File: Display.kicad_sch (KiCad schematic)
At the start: 28 parts, among them J10 Conn_01x06_MountingPin, J2 TFT_LCD, U3 MT9284, U5 TPS61169

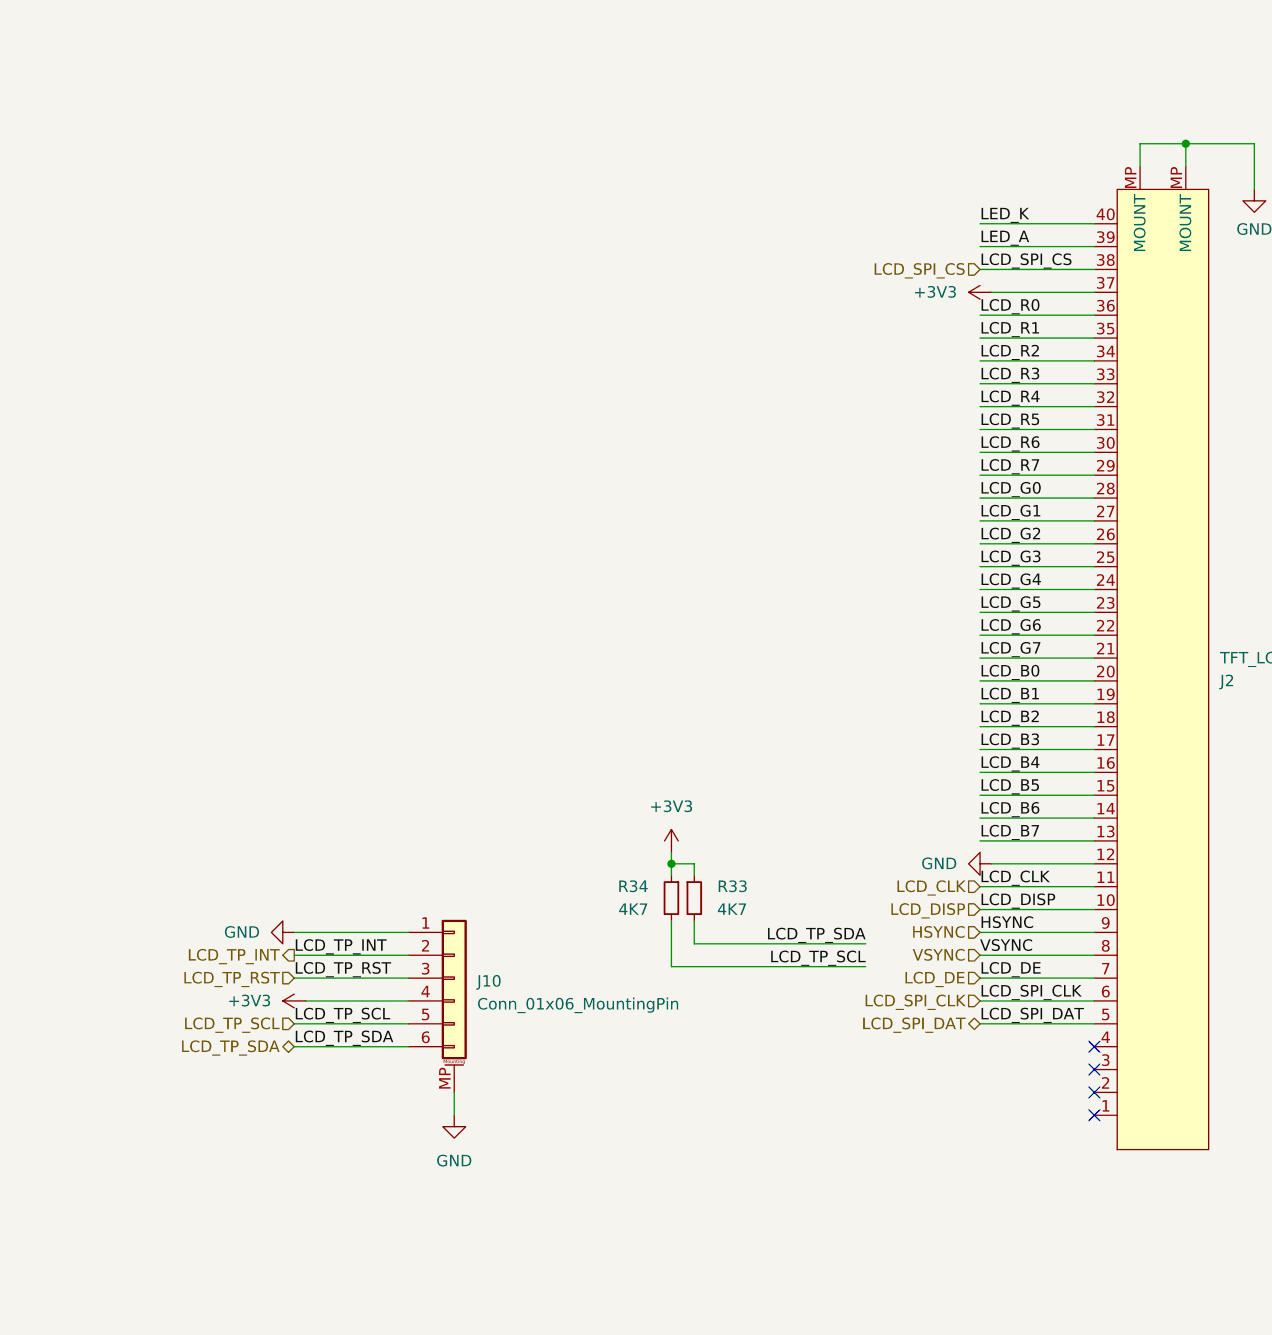
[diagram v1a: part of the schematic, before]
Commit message: Cleaning schematic, added more independently schematics
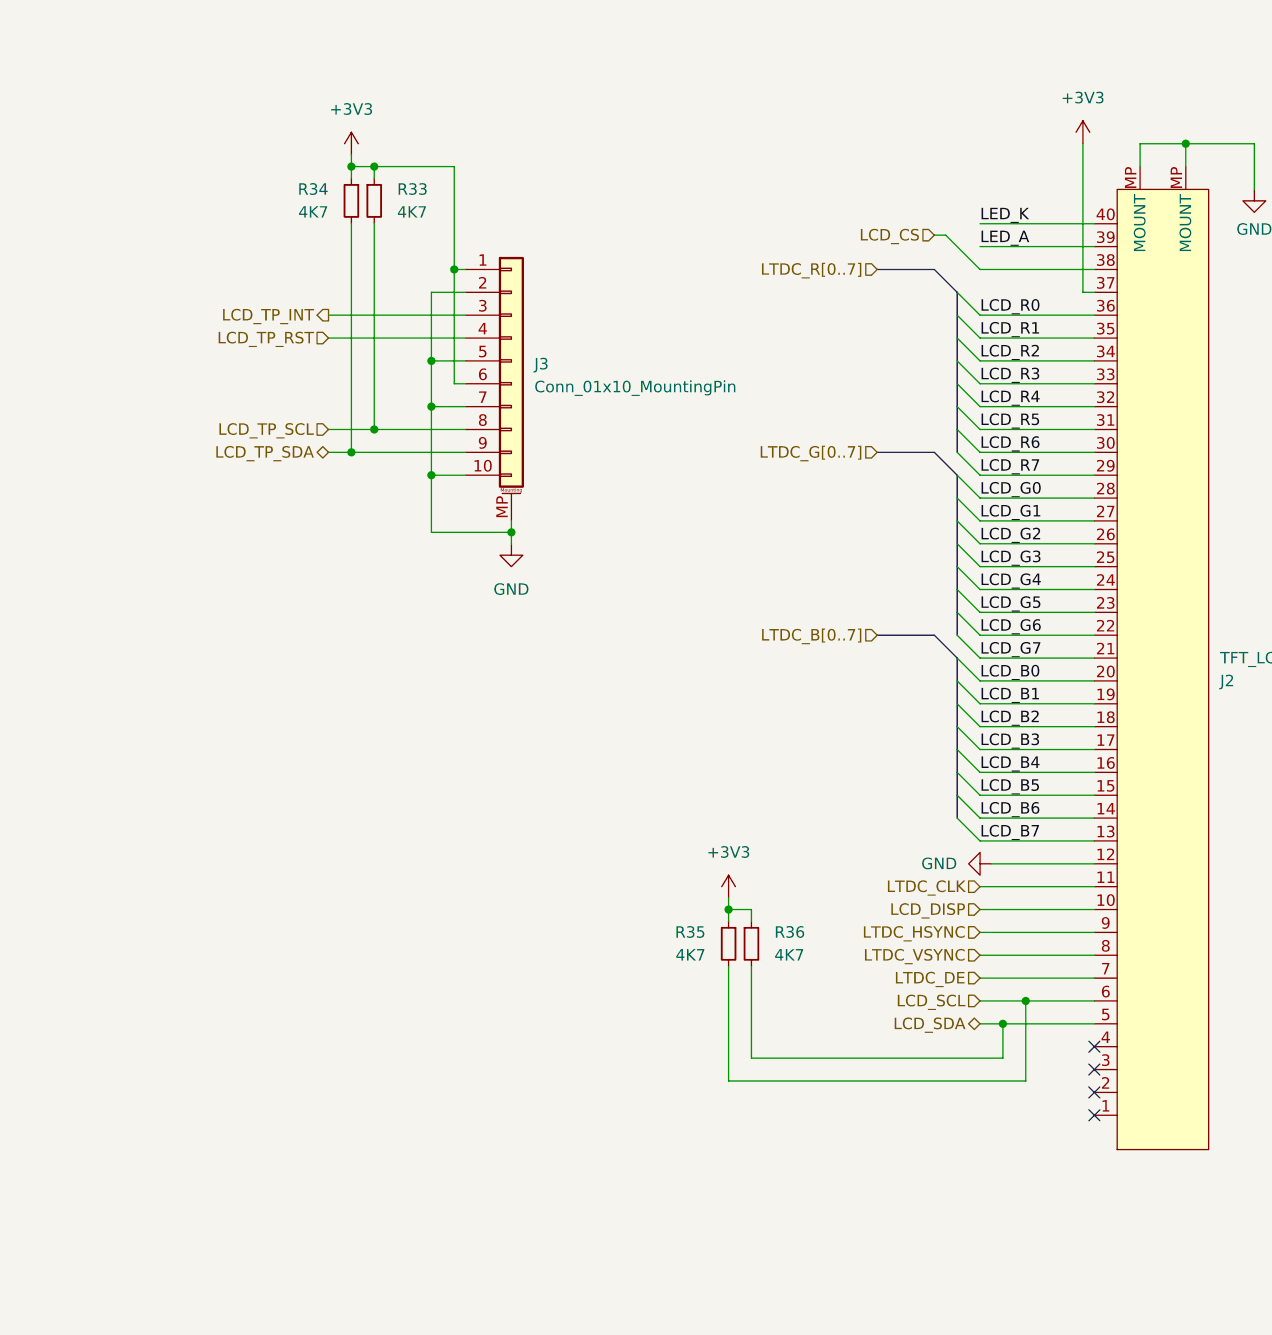
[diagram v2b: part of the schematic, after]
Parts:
- removed J10: Conn_01x06_MountingPin, Connector_FFC-FPC:TE_84953-6_1x06-1MP_P1.0mm_Horizontal, symbol Connector_Generic_MountingPin:Conn_01x06_MountingPin
- added J3: Conn_01x10_MountingPin, symbol Connector_Generic_MountingPin:Conn_01x10_MountingPin
- added R35, R36: 4K7, Resistor_SMD:R_0402_1005Metric, symbol Device:R_Small
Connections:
- net +3V3: now also J3.1 (Pin_1), J3.6 (Pin_6), R35.1, R36.1
- net GND: now also J3.10 (Pin_10), J3.2 (Pin_2), J3.5 (Pin_5), J3.7 (Pin_7), J3.MP (MountPin)
- net LCD_TP_INT: now also J3.3 (Pin_3)
- net LCD_TP_RST: now also J3.4 (Pin_4)
- net LCD_TP_SCL: now also R33.2, J3.8 (Pin_8); no longer R34.2
- net LCD_TP_SDA: now also R34.2, J3.9 (Pin_9); no longer R33.2
- net HSYNC renamed LTDC_HSYNC
- net LCD_CLK renamed LTDC_CLK
- net LCD_DE renamed LTDC_DE
- net LCD_SPI_CLK renamed LCD_SCL
- net LCD_SCL: now also R35.2
- net LCD_SPI_CS renamed LCD_CS
- net LCD_SPI_DAT renamed LCD_SDA
- net LCD_SDA: now also R36.2
- net VSYNC renamed LTDC_VSYNC
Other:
- moved on the sheet: R33, R34

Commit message: Layout SDRAM
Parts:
- J3: footprint (none) -> Connector_FFC-FPC:Hirose_FH12-10S-0.5SH_1x10-1MP_P0.50mm_Horizontal
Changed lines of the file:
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@@
 			)
 		)
-		(property "Footprint" ""
+		(property "Footprint" "Connector_FFC-FPC:Hirose_FH12-10S-0.5SH_1x10-1MP_P0.50mm_Horizontal"
 			(at 194.31 63.5 0)
 			(effects

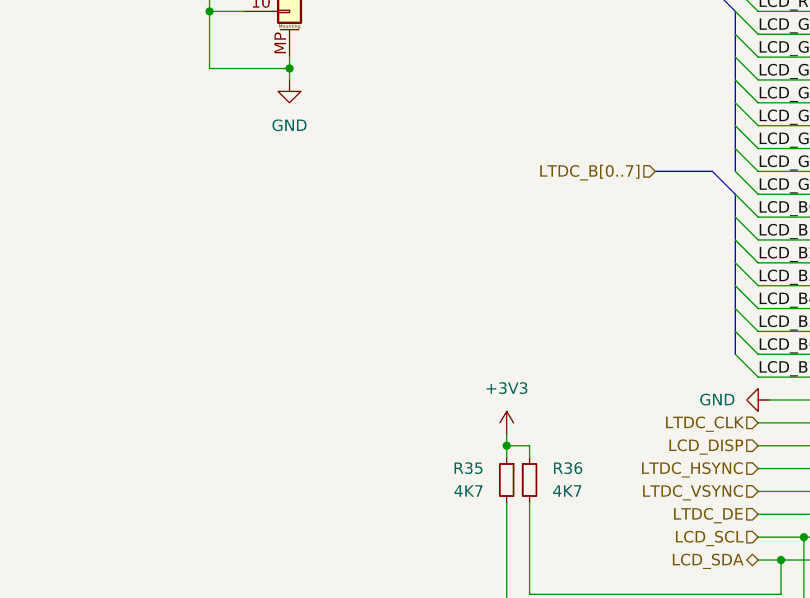
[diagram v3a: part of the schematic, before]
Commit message: relayout SDRAM
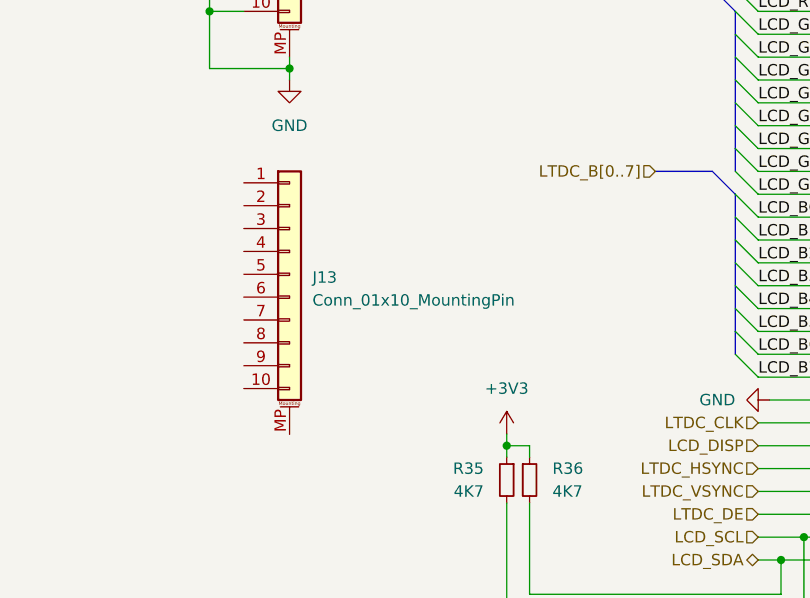
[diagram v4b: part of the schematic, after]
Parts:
- added J13: Conn_01x10_MountingPin, Connector_FFC-FPC:Hirose_FH12-10S-0.5SH_1x10-1MP_P0.50mm_Horizontal, symbol Connector_Generic_MountingPin:Conn_01x10_MountingPin
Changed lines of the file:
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@@
+	)
+	(symbol
+		(lib_id "Connector_Generic_MountingPin:Conn_01x10_MountingPin")
+		(at 194.31 105.41 0)
+		(unit 1)
+		(exclude_from_sim no)
+		(in_bom yes)
+		(on_board yes)
+		(dnp no)
+		(fields_autoplaced yes)
+		(property "Reference" "J13"
+			(at 196.85 105.7655 0)
+			(effects
+				(font
+					(size 1.27 1.27)
+				)
+				(justify left)
+			)
+		)
+		(property "Value" "Conn_01x10_MountingPin"
+			(at 196.85 108.3055 0)
+			(effects
+				(font
+					(size 1.27 1.27)
+				)
+				(justify left)
+			)
+		)
+		(property "Footprint" "Connector_FFC-FPC:Hirose_FH12-10S-0.5SH_1x10-1MP_P0.50mm_Horizontal"
+			(at 194.31 105.41 0)
+			(effects
+				(font
+					(size 1.27 1.27)
+				)
+				(hide yes)
+			)
+		)
+		(property "Datasheet" "~"
+			(at 194.31 105.41 0)
+			(effects
+				(font
+					(size 1.27 1.27)
+				)
+				(hide yes)
+			)
+		)
+		(property "Description" "Generic connectable mounting pin connector, single row, 01x10, script generated (kicad-library-utils/schlib/autogen/connector/)"
+			(at 194.31 105.41 0)
+			(effects
+				(font
+					(size 1.27 1.27)
+				)
+				(hide yes)
+			)
+		)
+		(pin "2"
+		)
+		(pin "1"
+		)
+		(pin "8"
+		)
+		(pin "3"
+		)
+		(pin "10"
+		)
+		(pin "4"
+		)
+		(pin "7"
+		)
+		(pin "9"
+		)
+		(pin "5"
+		)
+		(pin "MP"
+		)
+		(pin "6"
+		)
+		(instances
+			(project "chroma-pixel-zeta"
+				(path "/70094798-b7e4-48a4-a512-b8f48be18f9f/99abf84f-89dd-4209-b43f-cdbcbe391aaa"
+					(reference "J13")
+					(unit 1)
+				)
+			)
+		)
 	)
 	(symbol

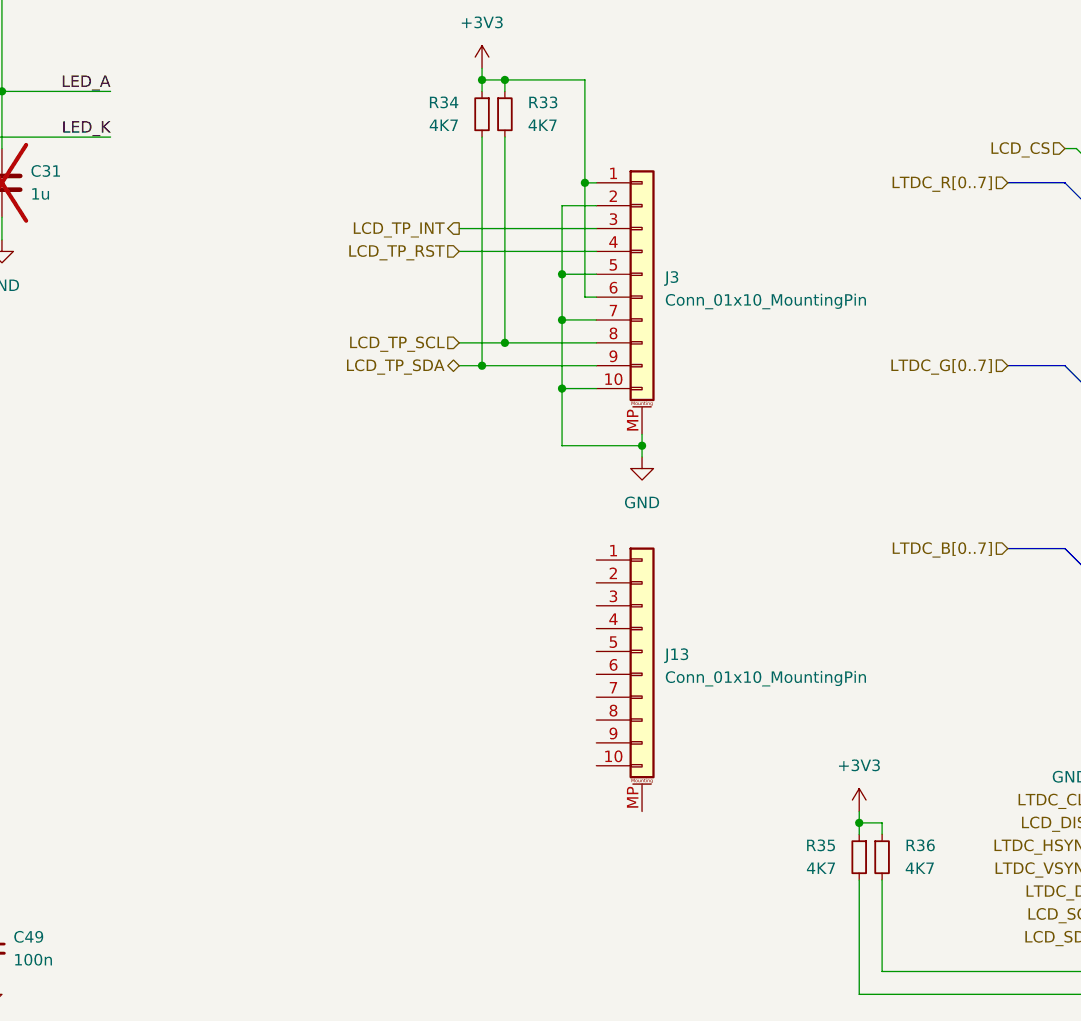
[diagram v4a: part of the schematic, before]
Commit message: Finished SDRAM, QSPI Flash, Planning to move to 5 inch orient display dimension
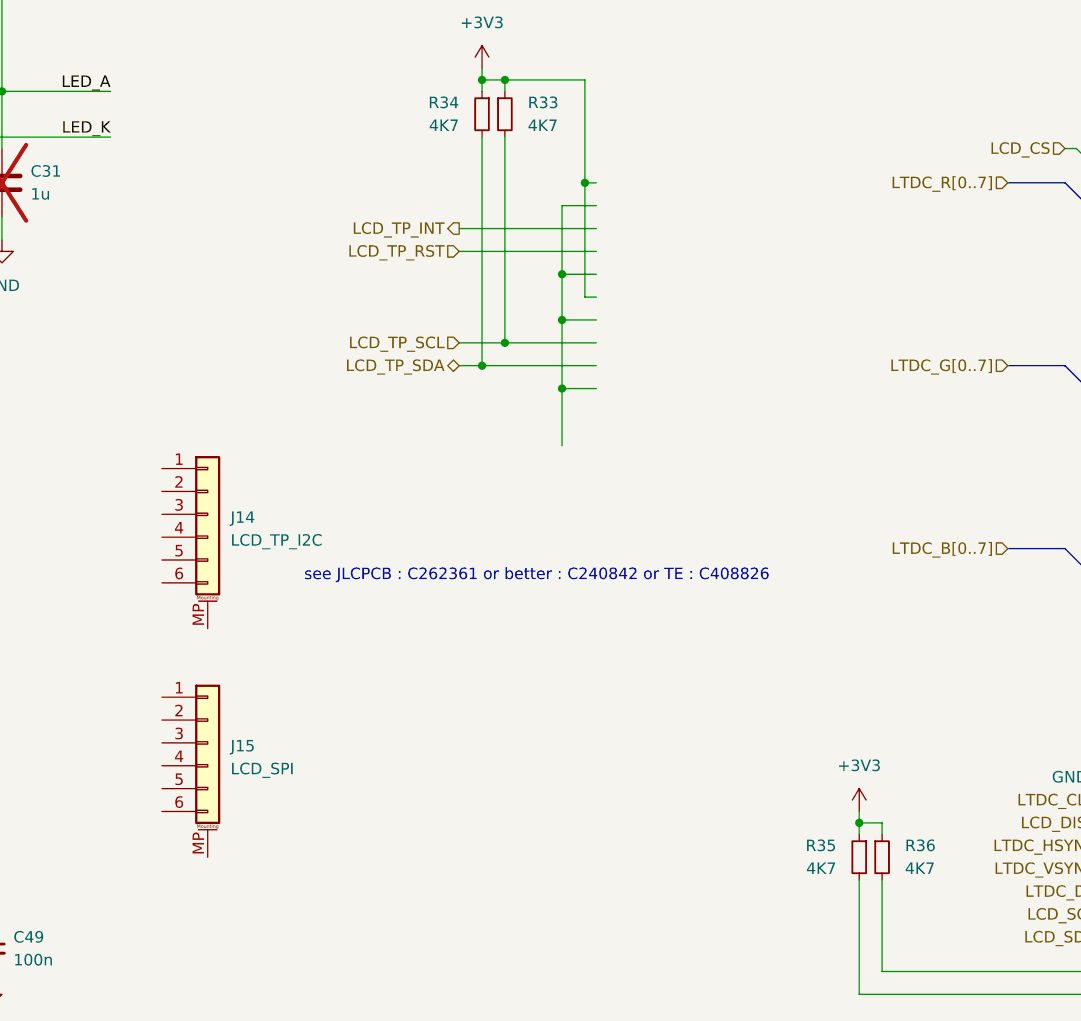
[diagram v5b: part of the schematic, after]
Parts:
- removed J13, J3: Conn_01x10_MountingPin, Connector_FFC-FPC:Hirose_FH12-10S-0.5SH_1x10-1MP_P0.50mm_Horizontal, symbol Connector_Generic_MountingPin:Conn_01x10_MountingPin
- added J14: LCD_TP_I2C, Connector_FFC-FPC:TE_84952-6_1x06-1MP_P1.0mm_Horizontal, symbol Connector_Generic_MountingPin:Conn_01x06_MountingPin
- added J15: LCD_SPI, Connector_FFC-FPC:TE_84952-6_1x06-1MP_P1.0mm_Horizontal, symbol Connector_Generic_MountingPin:Conn_01x06_MountingPin
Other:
- note added: "see JLCPCB : C262361 or better : C240842 or TE : C408826"
